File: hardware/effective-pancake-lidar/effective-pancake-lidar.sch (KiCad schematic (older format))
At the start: 20 parts, among them U2 R-78C5.0-1.0

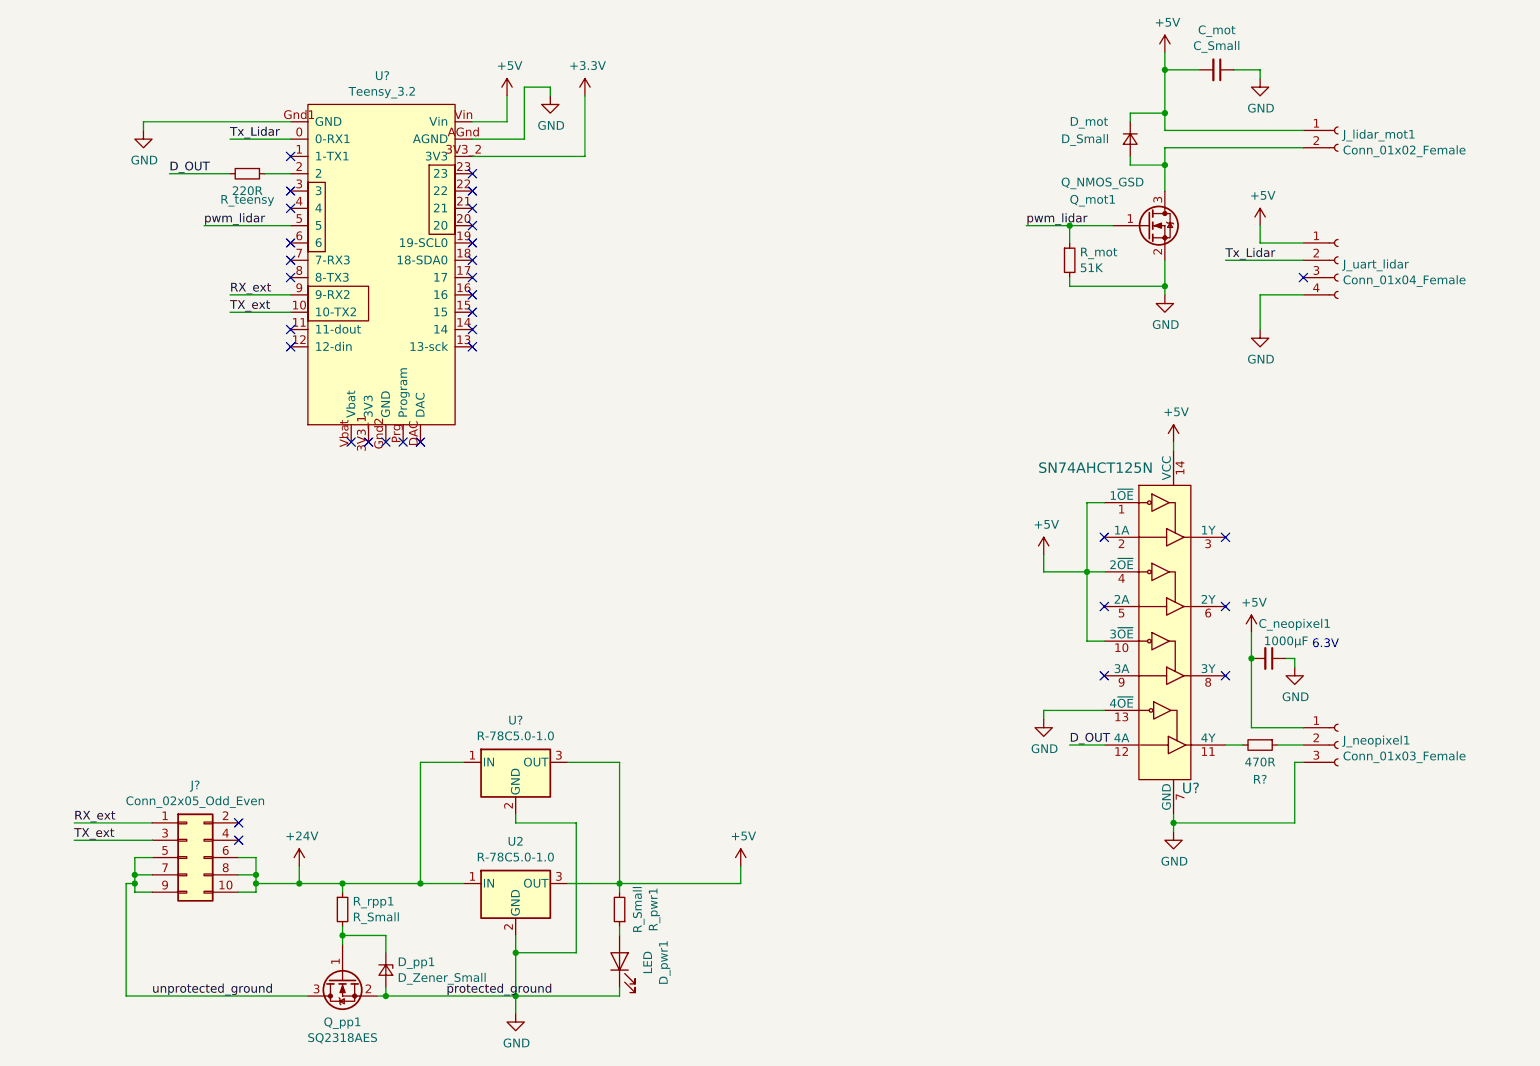
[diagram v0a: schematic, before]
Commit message: Finished schematics, fp association, and verifications.
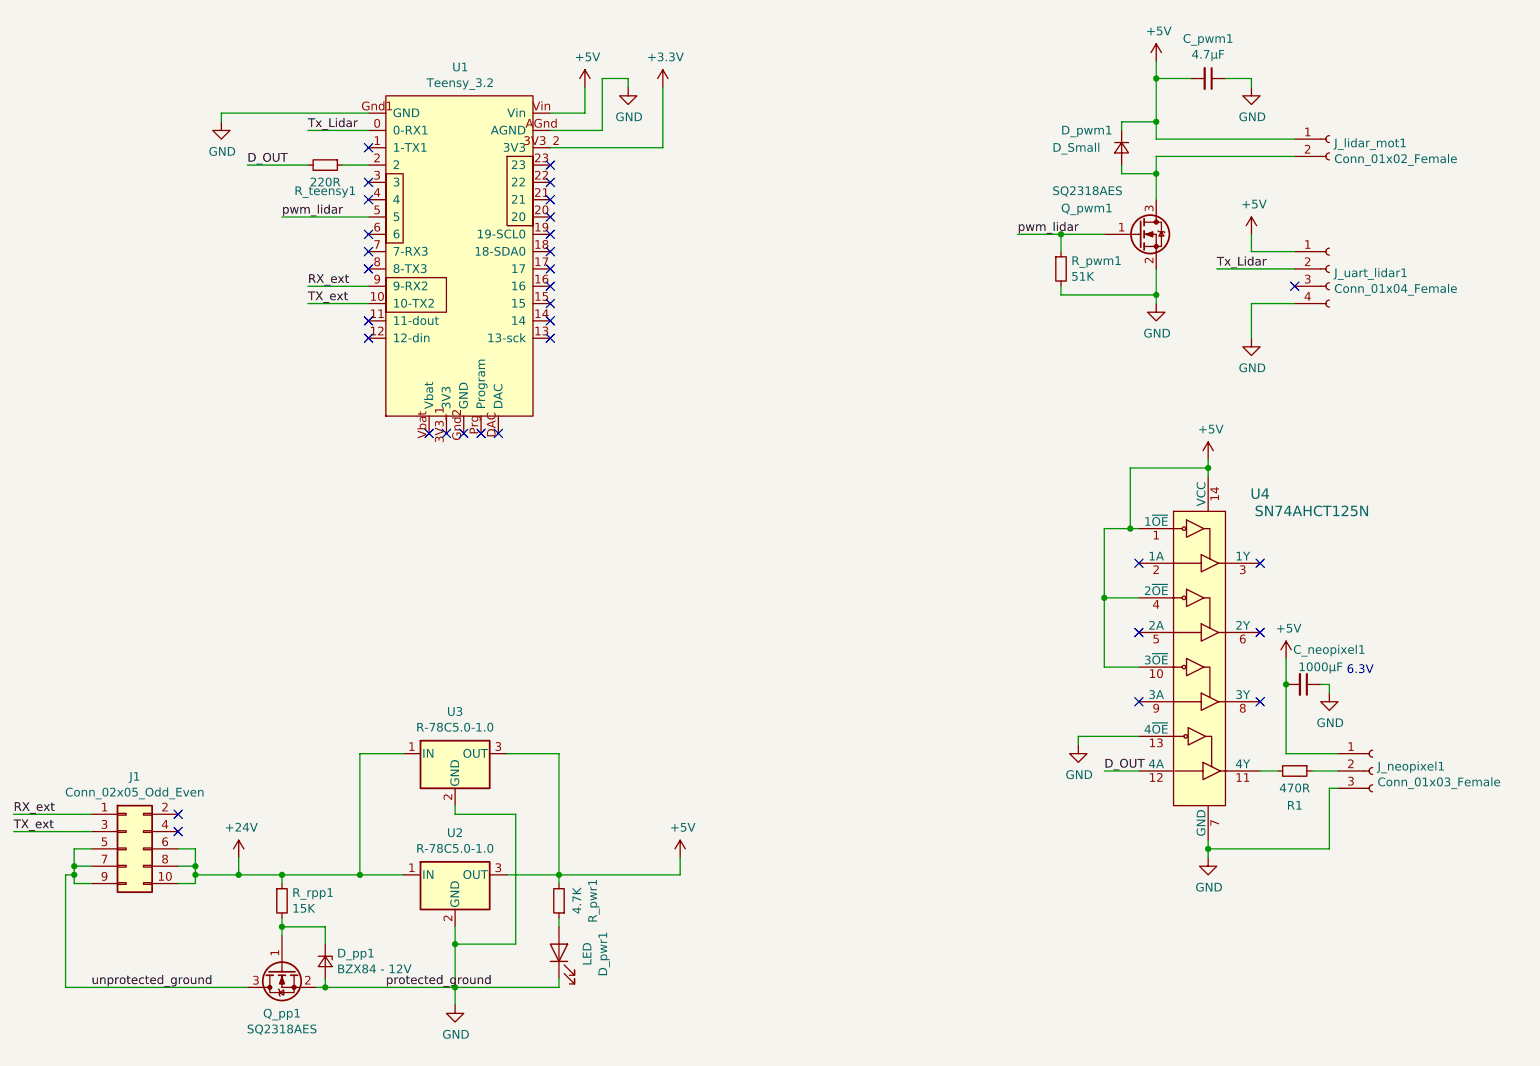
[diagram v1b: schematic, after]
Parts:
- removed U?: SN74AHCT125N, digikey-footprints:DIP-14_W3mm, symbol dk_Logic-Buffers-Drivers-Receivers-Transceivers:SN74AHCT125N
- added U4: SN74AHCT125N, digikey-footprints:DIP-14_W3mm, symbol dk_Logic-Buffers-Drivers-Receivers-Transceivers:SN74AHCT125N
- C_neopixel1: footprint (none) -> Capacitor_THT:C_Radial_D8.0mm_H11.5mm_P3.50mm
- C_pwm1: renamed from C_mot; value C_Small -> 4.7µF; footprint (none) -> Capacitor_THT:C_Radial_D4.0mm_H7.0mm_P1.50mm
- D_pp1: value D_Zener_Small -> BZX84 - 12V; footprint (none) -> Diode_SMD:D_SOT-23_ANK
- D_pwm1: renamed from D_mot; footprint (none) -> Diode_SMD:D_1206_3216Metric_Pad1.42x1.75mm_HandSolder
- D_pwr1: footprint (none) -> LED_SMD:LED_1206_3216Metric_Castellated
- J1: renamed from J?; footprint (none) -> Connector_IDC:IDC-Header_2x05_P2.54mm_Vertical
- J_lidar_mot1: footprint (none) -> Connector_JST:JST_XH_B2B-XH-A_1x02_P2.50mm_Vertical
- J_neopixel1: footprint (none) -> Connector_JST:JST_XH_B3B-XH-A_1x03_P2.50mm_Vertical
- J_uart_lidar1: renamed from J_uart_lidar; footprint (none) -> Connector_JST:JST_XH_B4B-XH-A_1x04_P2.50mm_Vertical
- Q_pp1: footprint (none) -> Package_TO_SOT_SMD:SOT-23
- Q_pwm1: renamed from Q_mot1; value Q_NMOS_GSD -> SQ2318AES; footprint (none) -> Package_TO_SOT_SMD:SOT-23
- R1: renamed from R?; footprint (none) -> Resistor_SMD:R_1206_3216Metric_Pad1.42x1.75mm_HandSolder
- R_pwm1: renamed from R_mot; footprint (none) -> Resistor_SMD:R_0805_2012Metric_Pad1.15x1.40mm_HandSolder
- R_pwr1: value R_Small -> 4.7K; footprint (none) -> Resistor_SMD:R_0805_2012Metric_Pad1.15x1.40mm_HandSolder
- R_rpp1: value R_Small -> 15K; footprint (none) -> Resistor_SMD:R_0805_2012Metric_Pad1.15x1.40mm_HandSolder
- R_teensy1: renamed from R_teensy; footprint (none) -> Resistor_SMD:R_1206_3216Metric
- U1: renamed from U?; footprint (none) -> digikey-footprints:Teensy_3.2
- gave numbers to parts that had none: 1
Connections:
- net +5V: now also U4.1 (1~OE), U4.10 (3~OE), U4.14 (VCC), U4.4 (2~OE)
- net D_OUT: now also U4.12 (4A)
- net GND: now also U4.13 (4~OE), U4.7 (GND)
- net at R1.2: now also U4.11 (4Y)
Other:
- moved on the sheet: C_neopixel1, C_pwm1, D_pp1, D_pwm1, D_pwr1, J1, J_lidar_mot1, J_neopixel1, J_uart_lidar1, Q_pp1, Q_pwm1, R1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
